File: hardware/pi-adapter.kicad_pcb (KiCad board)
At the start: 2 copper layers, 64 x 56 mm, 37 parts, among them P1 CONN_02X20, P10 CONN_01X04, P100 CONN_01X01, P101 CONN_01X01, P103 CONN_01X01, P11 CONN_01X04, P12 CONN_01X04, P13 CONN_01X04, P14 CONN_01X04, P15 CONN_01X04, P16 CONN_01X04, P17 CONN_01X04, P18 CONN_01X04, P19 CONN_01X04, P2 +5V, P20 CONN_01X04, P21 CONN_01X04, P22 CONN_01X06, P3 CONN_01X03, P4 GND, P5 CONN_01X03, P6 CONN_01X04, P7 CONN_01X04, P8 CONN_01X04, P9 CONN_01X04, U1 74HCT245, U2 74HCT245, U3 74HCT245, U4 74HCT245

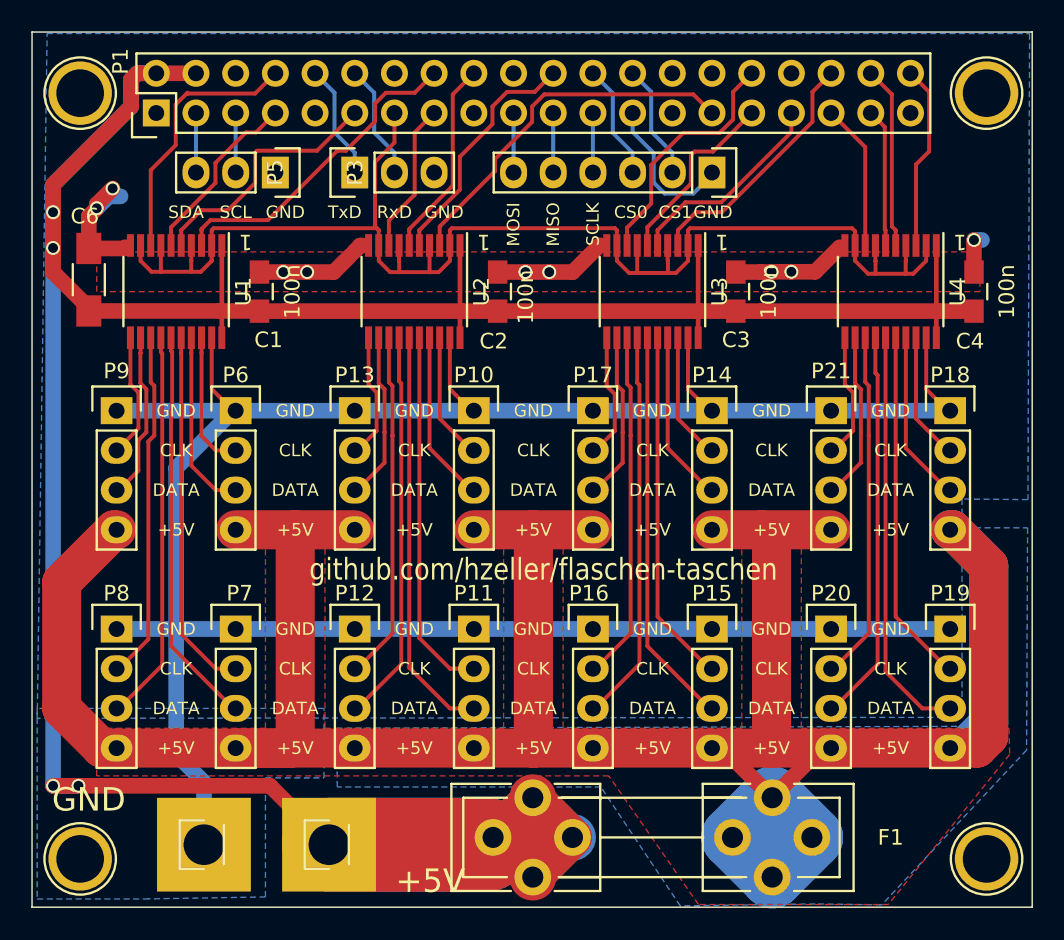
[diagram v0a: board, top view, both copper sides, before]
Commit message: o Moar copper on 5V fused (with diminishing returns)
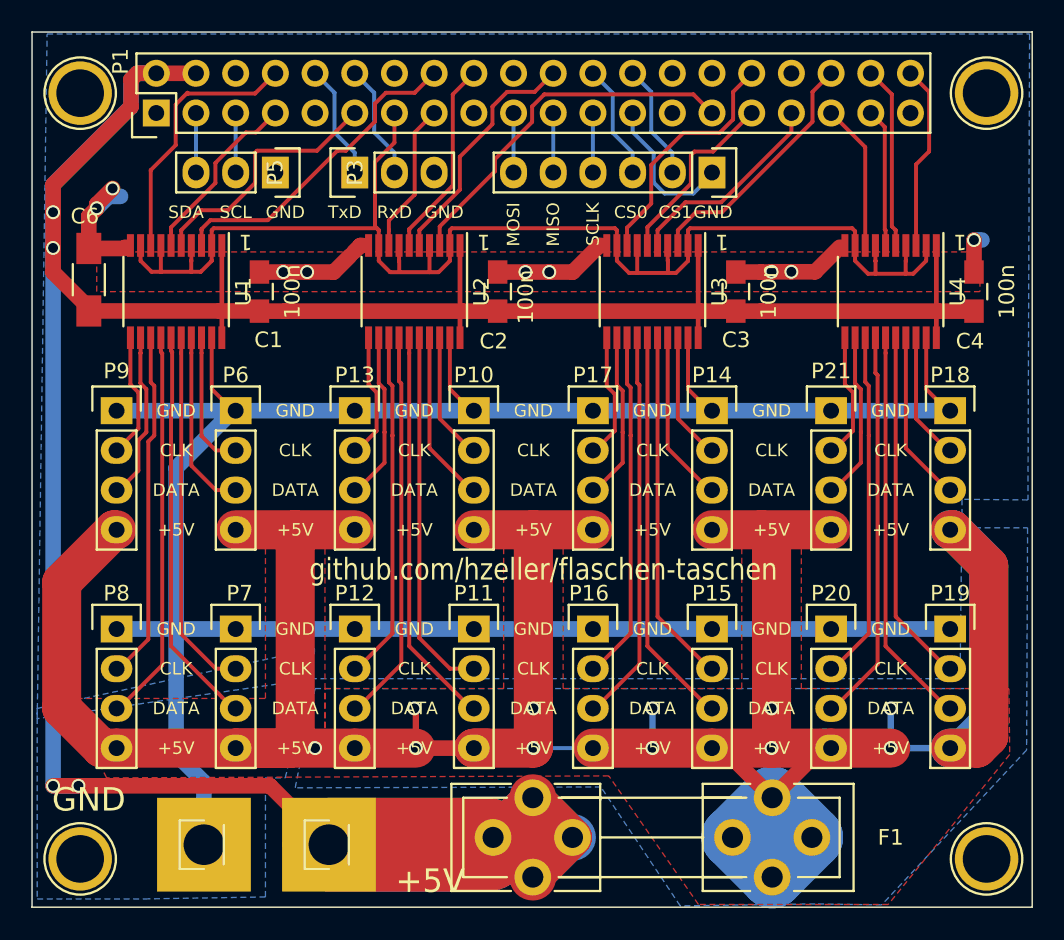
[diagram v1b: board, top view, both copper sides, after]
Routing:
- net Fused5V: track 199.4 -> 222.3 mm, vias 0 -> 11
- net Net-(P19-Pad3): track 26.5 -> 25.5 mm
- net Net-(P11-Pad3): track 26.3 -> 25.5 mm
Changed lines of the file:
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@@
     (thickness 1.6)
     (drawings 80)
-    (tracks 539)
+    (tracks 565)
     (zones 0)
     (modules 37)
@@
   )
   (setup
-    (last_trace_width 3)
+    (last_trace_width 0.254)
     (user_trace_width 0.254)
     (user_trace_width 0.3048)
@@
   (segment (start 126.746 78.74) (end 128.27 78.74) (width 0.254) (layer F.Cu) (net 34))
   (segment (start 124.785 57.56) (end 124.785 76.779) (width 0.254) (layer F.Cu) (net 34))
-  (segment (start 124.135 78.669) (end 126.746 81.28) (width 0.254) (layer F.Cu) (net 35))
-  (segment (start 126.746 81.28) (end 128.27 81.28) (width 0.254) (layer F.Cu) (net 35))
-  (segment (start 124.135 57.56) (end 124.135 78.669) (width 0.254) (layer F.Cu) (net 35))
+  (segment (start 128.27 81.28) (end 128.1176 81.28) (width 0.254) (layer F.Cu) (net 35))
+  (segment (start 128.1176 81.28) (end 124.135 77.2974) (width 0.254) (layer F.Cu) (net 35))
+  (segment (start 124.135 77.2974) (end 124.135 58.539) (width 0.254) (layer F.Cu) (net 35))
+  (segment (start 124.135 58.539) (end 124.135 57.56) (width 0.254) (layer F.Cu) (net 35))
   (segment (start 123.063 63.819274) (end 123.063 76.4794) (width 0.254) (layer F.Cu) (net 36))
   (segment (start 123.063 76.4794) (end 120.8024 78.74) (width 0.254) (layer F.Cu) (net 36))
@@
   (segment (start 158.5976 78.74) (end 158.75 78.74) (width 0.254) (layer F.Cu) (net 50))
   (segment (start 155.265 75.4074) (end 158.5976 78.74) (width 0.254) (layer F.Cu) (net 50))
-  (segment (start 154.615 78.923) (end 156.972 81.28) (width 0.254) (layer F.Cu) (net 51))
-  (segment (start 156.972 81.28) (end 158.75 81.28) (width 0.254) (layer F.Cu) (net 51))
-  (segment (start 154.615 57.56) (end 154.615 78.923) (width 0.254) (layer F.Cu) (net 51))
+  (segment (start 158.75 81.28) (end 158.5976 81.28) (width 0.254) (layer F.Cu) (net 51))
+  (segment (start 158.5976 81.28) (end 154.615 77.2974) (width 0.254) (layer F.Cu) (net 51))
+  (segment (start 154.615 58.539) (end 154.615 57.56) (width 0.254) (layer F.Cu) (net 51))
+  (segment (start 154.615 77.2974) (end 154.615 58.539) (width 0.254) (layer F.Cu) (net 51))
   (segment (start 153.543 63.819274) (end 153.543 76.4794) (width 0.254) (layer F.Cu) (net 52))
   (segment (start 153.543 76.4794) (end 151.2824 78.74) (width 0.254) (layer F.Cu) (net 52))
@@
   (segment (start 153.034989 65.557411) (end 151.2824 67.31) (width 0.254) (layer F.Cu) (net 55))
   (segment (start 151.2824 67.31) (end 151.13 67.31) (width 0.254) (layer F.Cu) (net 55))
+  (segment (start 154.948807 83.82) (end 154.948807 81.288807) (width 0.4064) (layer B.Cu) (net 56))
+  (segment (start 154.948807 81.288807) (end 154.94 81.28) (width 0.4064) (layer B.Cu) (net 56))
+  (via (at 154.94 81.28) (size 0.889) (drill 0.635) (layers F.Cu B.Cu) (net 56))
+  (segment (start 151.13 83.82) (end 154.948807 83.82) (width 2.5) (layer F.Cu) (net 56))
+  (segment (start 158.75 83.82) (end 154.948807 83.82) (width 0.4064) (layer B.Cu) (net 56))
+  (via (at 154.948807 83.82) (size 0.889) (drill 0.635) (layers F.Cu B.Cu) (net 56))
+  (segment (start 139.7 83.82) (end 139.7 81.28) (width 0.4064) (layer B.Cu) (net 56))
+  (via (at 139.7 81.28) (size 0.889) (drill 0.635) (layers F.Cu B.Cu) (net 56))
+  (segment (start 143.51 83.82) (end 139.7 83.82) (width 0.4064) (layer B.Cu) (net 56))
+  (via (at 139.7 83.82) (size 0.889) (drill 0.635) (layers F.Cu B.Cu) (net 56))
+  (segment (start 124.558467 83.82) (end 124.558467 81.378467) (width 0.4064) (layer F.Cu) (net 56))
+  (segment (start 124.558467 81.378467) (end 124.46 81.28) (width 0.4064) (layer F.Cu) (net 56))
+  (via (at 124.46 81.28) (size 0.889) (drill 0.635) (layers F.Cu B.Cu) (net 56))
+  (segment (start 120.65 83.82) (end 124.558467 83.82) (width 2.5) (layer F.Cu) (net 56))
+  (segment (start 128.27 83.82) (end 124.558467 83.82) (width 1) (layer F.Cu) (net 56))
+  (via (at 124.558467 83.82) (size 0.889) (drill 0.635) (layers F.Cu B.Cu) (net 56))
+  (segment (start 120.65 83.82) (end 118.11 83.82) (width 0.254) (layer B.Cu) (net 56))
+  (via (at 118.11 83.82) (size 0.889) (drill 0.635) (layers F.Cu B.Cu) (net 56))
+  (segment (start 147.32 83.82) (end 147.32 81.28) (width 0.254) (layer B.Cu) (net 56))
+  (via (at 147.32 81.28) (size 0.889) (drill 0.635) (layers F.Cu B.Cu) (net 56))
+  (segment (start 151.13 83.82) (end 147.32 83.82) (width 0.254) (layer B.Cu) (net 56))
+  (via (at 147.32 83.82) (size 0.889) (drill 0.635) (layers F.Cu B.Cu) (net 56))
+  (segment (start 132.08 83.82) (end 132.08 81.28) (width 0.254) (layer B.Cu) (net 56))
+  (via (at 132.08 81.28) (size 0.889) (drill 0.635) (layers F.Cu B.Cu) (net 56))
+  (segment (start 135.89 83.82) (end 135.7376 83.82) (width 0.254) (layer B.Cu) (net 56))
+  (via (at 132.08 83.82) (size 0.889) (drill 0.635) (layers F.Cu B.Cu) (net 56))
+  (segment (start 135.7376 83.82) (end 132.08 83.82) (width 0.254) (layer B.Cu) (net 56))
   (segment (start 161.21601 83.08119) (end 160.4772 83.82) (width 2.5) (layer F.Cu) (net 56))
   (segment (start 158.9024 69.85) (end 161.21601 72.16361) (width 2.5) (layer F.Cu) (net 56))
@@
   (segment (start 150.53564 83.82) (end 147.36064 86.995) (width 1) (layer F.Cu) (net 56))
   (segment (start 128.27 83.82) (end 132.08 83.82) (width 2.5) (layer F.Cu) (net 56))
-  (segment (start 132.08 83.82) (end 135.89 83.82) (width 2.5) (layer F.Cu) (net 56))
   (segment (start 132.08 80.894338) (end 132.08 83.82) (width 2.5) (layer F.Cu) (net 56))
   (segment (start 143.51 69.85) (end 146.685 69.85) (width 2.5) (layer F.Cu) (net 56))
@@
   (segment (start 113.03 69.85) (end 116.84 69.85) (width 2.5) (layer F.Cu) (net 56))
   (segment (start 116.84 69.85) (end 120.65 69.85) (width 2.5) (layer F.Cu) (net 56))
-  (segment (start 151.13 83.82) (end 158.75 83.82) (width 2.5) (layer F.Cu) (net 56))
   (segment (start 135.89 83.82) (end 143.51 83.82) (width 2.5) (layer F.Cu) (net 56))
-  (segment (start 120.65 83.82) (end 128.27 83.82) (width 2.5) (layer F.Cu) (net 56))
   (segment (start 113.03 83.82) (end 120.65 83.82) (width 2.5) (layer F.Cu) (net 56))
   (segment (start 105.41 83.82) (end 113.03 83.82) (width 2.5) (layer F.Cu) (net 56))
@@
     (polygon
       (pts
-        (xy 118.745 82.55) (xy 130.175 82.55) (xy 130.175 69.215) (xy 133.985 69.215) (xy 133.985 82.55)
-        (xy 145.415 82.55) (xy 145.415 69.215) (xy 149.225 69.215) (xy 149.225 82.55) (xy 162.5092 82.55)
-        (xy 162.56 84.2264) (xy 154.7876 93.8276) (xy 142.6464 93.8276) (xy 136.906 85.598) (xy 104.14 85.598)
-        (xy 104.14 82.55) (xy 114.935 82.55) (xy 114.935 69.215) (xy 118.745 69.215) (xy 118.745 82.55)
+        (xy 118.745 80.01) (xy 130.175 80.01) (xy 130.175 69.215) (xy 133.985 69.215) (xy 133.985 80.01)
+        (xy 145.415 80.01) (xy 145.415 69.215) (xy 149.225 69.215) (xy 149.225 80.01) (xy 162.5092 80.01)
+        (xy 162.56 84.2264) (xy 154.7876 93.8276) (xy 142.6464 93.8276) (xy 136.906 85.598) (xy 104.775 85.725)
+        (xy 102.235 80.645) (xy 114.935 80.645) (xy 114.935 69.215) (xy 118.745 69.215) (xy 118.745 82.55)
       )
     )
@@
     (polygon
       (pts
-        (xy 119.492261 82.55) (xy 160.401 82.423) (xy 160.3375 69.723) (xy 163.703 69.723) (xy 163.6395 83.947)
-        (xy 154.3685 93.853) (xy 150.114 93.7895) (xy 141.478 93.9165) (xy 136.398 86.3092) (xy 119.5324 86.3092)
+        (xy 118.11 80.01) (xy 160.02 80.01) (xy 160.3375 69.723) (xy 163.703 69.723) (xy 163.6395 83.947)
+        (xy 154.3685 93.853) (xy 150.114 93.7895) (xy 141.478 93.9165) (xy 136.398 86.3092) (xy 116.84 86.36)
       )
     )
@@
     (polygon
       (pts
-        (xy 100.965 38.1) (xy 163.83 38.1) (xy 163.7284 67.9196) (xy 159.512 67.8815) (xy 159.512 81.8515)
-        (xy 100.33 81.915)
+        (xy 100.965 38.119407) (xy 163.83 38.119407) (xy 163.7284 67.939007) (xy 159.512 67.900907) (xy 159.385 79.375)
+        (xy 118.11 79.375) (xy 100.33 81.934407)
       )
     )
@@
     (polygon
       (pts
-        (xy 107.188 93.472) (xy 114.935 93.345) (xy 114.935 85.725) (xy 118.6815 85.725) (xy 118.6815 81.28)
+        (xy 107.188 93.472) (xy 114.935 93.345) (xy 114.935 85.725) (xy 116.205 85.725) (xy 118.11 77.47)
         (xy 100.33 81.28) (xy 100.33 93.472)
       )

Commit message: o Less vias where text is. o Moar copper.
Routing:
- net Fused5V: track 222.3 -> 234.3 mm, vias 11 -> 13
- added copper zone on B.Cu, net VCC
- added copper zone on F.Cu, net VCC

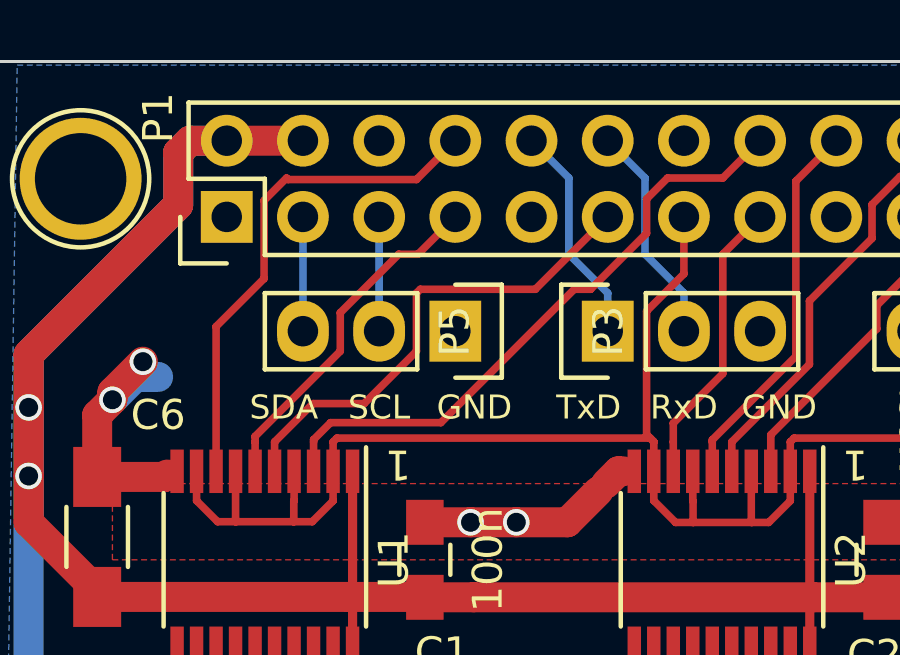
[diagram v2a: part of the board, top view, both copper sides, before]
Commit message: o Doh': serial interface connection was off by one pin.
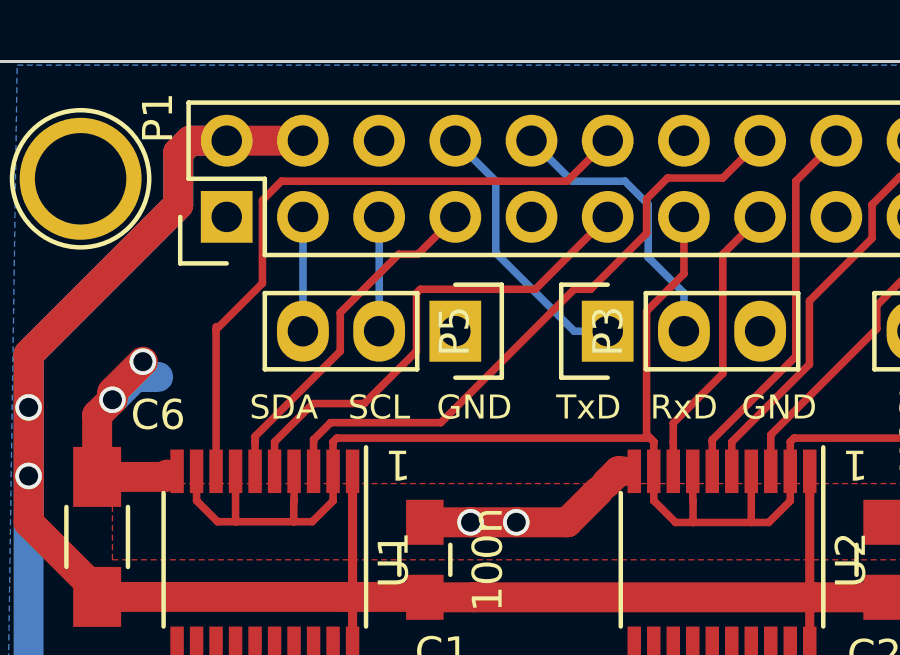
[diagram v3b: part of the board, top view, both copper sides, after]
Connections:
- P1 pad 12: Net-(P1-Pad12) -> D1
- P1 pad 30: (no net) -> GND
- P1 pad 8: D1 -> Net-(P1-Pad8)
- P5 pad 1: Net-(P1-Pad10) -> Net-(P1-Pad8)
- P5 pad 2: Net-(P1-Pad12) -> Net-(P1-Pad10)
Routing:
- net Net-(P1-Pad8): track 0.00 -> 9.11 mm
- net Net-(P1-Pad12): track 7.40 -> 0.00 mm
- net D1: track 16.9 -> 22.1 mm
- net Net-(P1-Pad10): track 7.40 -> 9.49 mm
